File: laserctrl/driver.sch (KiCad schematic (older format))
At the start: 21 parts, among them IC4 DRV8811, P1 CONN_4

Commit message: Deleted the A-axis, it's getting too cramped with limited 328 I/O
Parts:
- C35: renamed from C64; value 100nF -> 1nF
- C36: renamed from C52; value 100nF -> 1nF
- R28: renamed from R44; value 1k -> 33k
- R29: renamed from R37; value 1k -> 33k
- R30: renamed from R38; value R -> 0R22
- R31: renamed from R39; value R -> 0R22
- gave numbers to parts that had none: 4
- renumbered C61 to C33, C51 to C34, C53 to C37, C54 to C38, C55 to C39, IC4 to IC7, JP1 to JP7, JP2 to JP8, P1 to P10, RV1 to RV7, RV2 to RV8
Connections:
- wire segments 70 -> 71
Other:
- moved on the sheet: D2, P3, R8, R9

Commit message: Actually did some work
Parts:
- removed RV7, RV8: 10k, symbol POT
- added C?: 100nF, symbol C
- added D?: LED, symbol LED
- added P?: CONN_2, symbol CONN_2
- added R? (x3): 10k, symbol R
- added R?: 330, symbol R
- added R?: 1k, symbol R
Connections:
- net labels added: +3.3V, Current, Max-Limit, Min-Limit
- net labels removed: +5V, Limit
- wire segments 71 -> 85
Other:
- note removed: "Current"
- note removed: "Decay\nmode"
- moved on the sheet: C12, C18, D2, P3, P4, R8, R9

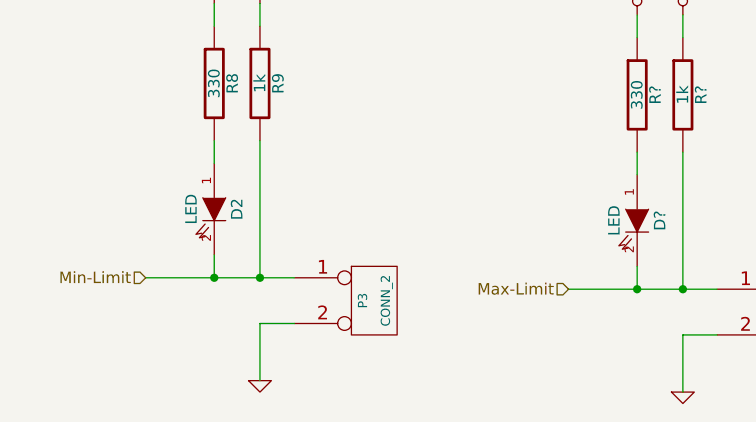
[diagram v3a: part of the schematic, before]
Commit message: Added laser interface schematic
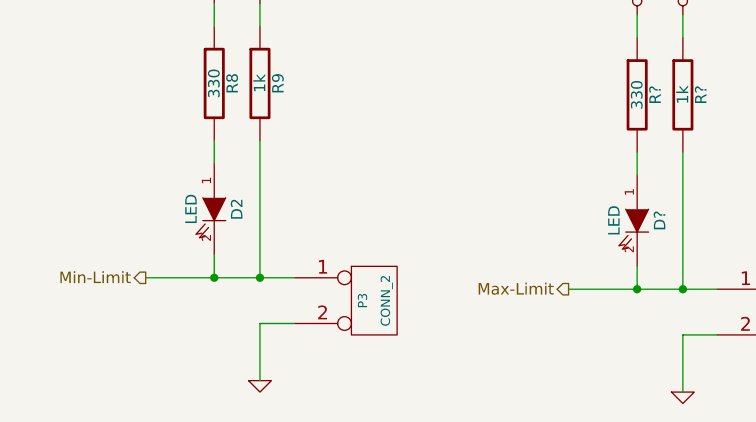
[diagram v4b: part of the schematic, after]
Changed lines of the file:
@@
-EESchema Schematic File Version 2  date 2011-10-30T14:11:45 CET
+EESchema Schematic File Version 2  date 2011-10-31T20:32:47 CET
 LIBS:power
 LIBS:device
@@
 EELAYER END
 $Descr A4 11700 8267
-Sheet 5 7
+Sheet 7 8
 Title ""
-Date "30 oct 2011"
+Date "31 oct 2011"
 Rev ""
 Comp ""
@@
 	0    1    1    0
 $EndComp
-Text HLabel 3400 7150 0    50   Input ~ 0
+Text HLabel 3400 7150 0    50   Output ~ 0
 Max-Limit
 $Comp
@@
 	-1   0    0    1
 $EndComp
-Text HLabel 1550 7100 0    50   Input ~ 0
+Text HLabel 1550 7100 0    50   Output ~ 0
 Min-Limit
 $Comp

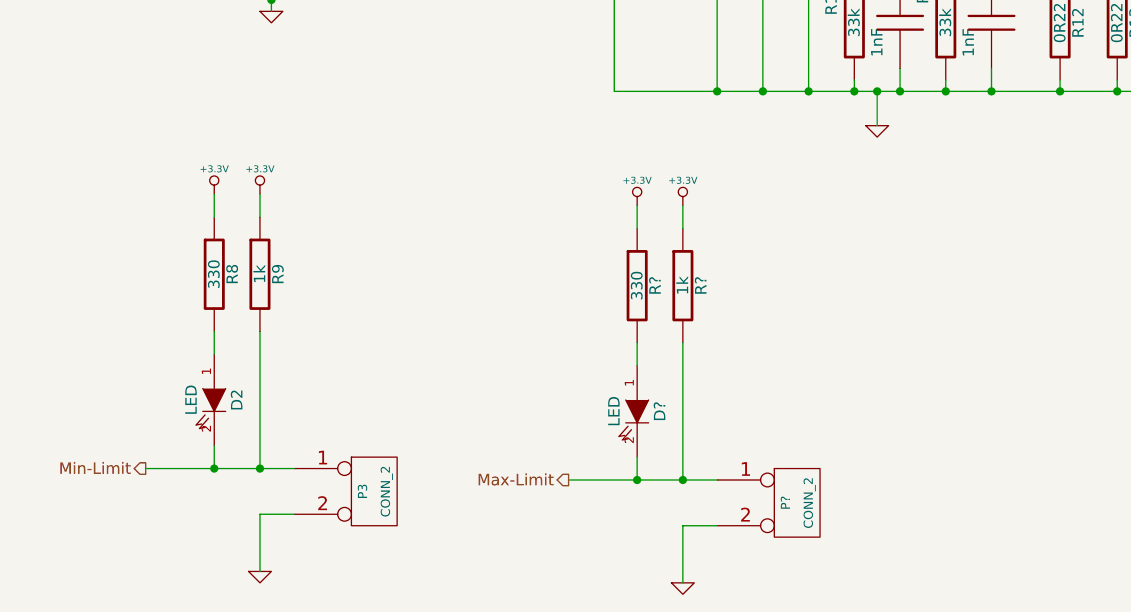
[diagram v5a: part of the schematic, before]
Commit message: Added transistors to drive the optocouplers
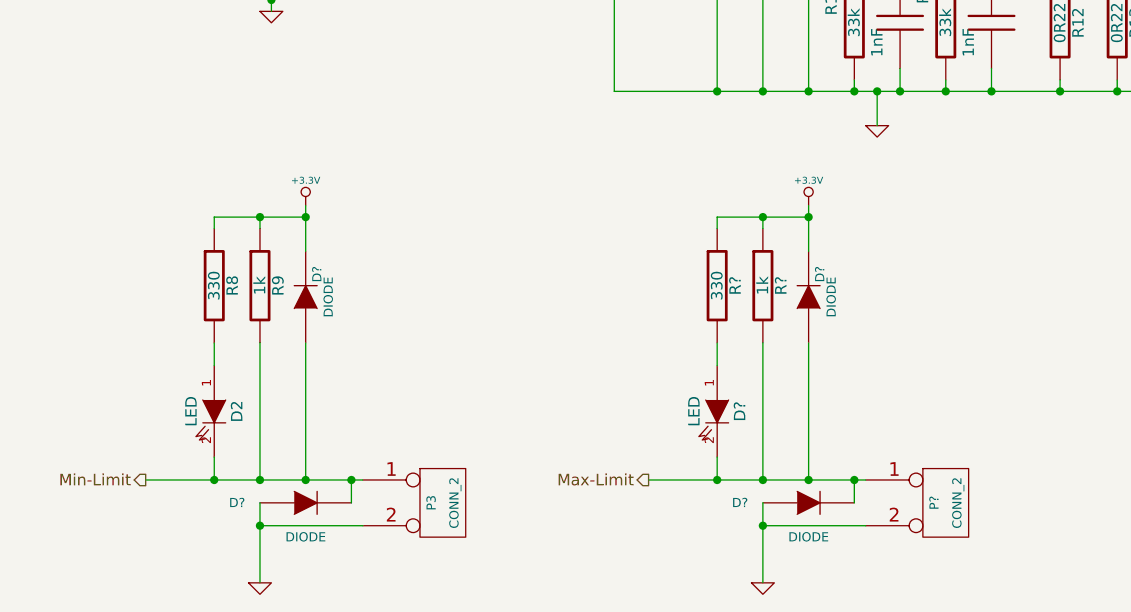
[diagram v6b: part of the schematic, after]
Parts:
- removed D?: LED, symbol LED
- removed P?: CONN_2, symbol CONN_2
- removed R?: 330, symbol R
- removed R?: 1k, symbol R
- added D? (x4): DIODE, symbol DIODE
- added D?: LED, symbol LED
- added P?: CONN_2, symbol CONN_2
- added R?: 330, symbol R
- added R?: 1k, symbol R
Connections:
- net +3.3V: now also D?.2 (K), D?.2 (K), R?.1, R?.1
- net GND: now also D?.1 (A), D?.1 (A), P?.2 (PM)
- net Max-Limit: now also D?.1 (A), D?.2 (K), D?.2 (K), P?.1 (P1), R?.2
- net Min-Limit: now also D?.1 (A), D?.2 (K)
- new net: D?.1 (A), R?.2
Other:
- moved on the sheet: D2, P3, R8, R9
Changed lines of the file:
@@
-EESchema Schematic File Version 2  date 2011-11-03T00:14:20 CET
+EESchema Schematic File Version 2  date 2011-11-04T21:23:22 CET
 LIBS:power
 LIBS:device
@@
 Sheet 7 8
 Title ""
-Date "2 nov 2011"
+Date "4 nov 2011"
 Rev ""
 Comp ""
@@
 Comment4 ""
 $EndDescr
+$Comp
+L GND #PWR?
+U 1 1 4EB44970
+P 4250 7600
+F 0 "#PWR?" H 4250 7600 30  0001 C CNN
+F 1 "GND" H 4250 7530 30  0001 C CNN
+	1    4250 7600
+	1    0    0    -1
+$EndComp
+$Comp
+L CONN_2 P?
+U 1 1 4EB4496F
+P 5050 7250
+F 0 "P?" V 5000 7250 40  0000 C CNN
+F 1 "CONN_2" V 5100 7250 40  0000 C CNN
+	1    5050 7250
+	1    0    0    -1
+$EndComp
+$Comp
+L R R?
+U 1 1 4EB4496E
+P 4250 6300
+F 0 "R?" V 4330 6300 50  0000 C CNN
+F 1 "1k" V 4250 6300 50  0000 C CNN
+	1    4250 6300
+	1    0    0    -1
+$EndComp
+$Comp
+L R R?
+U 1 1 4EB4496D
+P 4050 6300
+F 0 "R?" V 4130 6300 50  0000 C CNN
+F 1 "330" V 4050 6300 50  0000 C CNN
+	1    4050 6300
+	1    0    0    -1
+$EndComp
+$Comp
+L LED D?
+U 1 1 4EB4496C
+P 4050 6850
+F 0 "D?" H 4050 6950 50  0000 C CNN
+F 1 "LED" H 4050 6750 50  0000 C CNN
+	1    4050 6850
+	0    1    1    0
+$EndComp
+$Comp
+L +3.3V #PWR?
+U 1 1 4EB4496B
+P 4450 5950
+F 0 "#PWR?" H 4450 5910 30  0001 C CNN
+F 1 "+3.3V" H 4450 6060 30  0000 C CNN
+	1    4450 5950
+	1    0    0    -1
+$EndComp
+$Comp
+L DIODE D?
+U 1 1 4EB4496A
+P 4450 6350
+F 0 "D?" H 4550 6300 40  0000 C CNN
+F 1 "DIODE" H 4450 6250 40  0000 C CNN
+	1    4450 6350
+	0    -1   -1   0
+$EndComp
+$Comp
+L DIODE D?
+U 1 1 4EB44969
+P 4450 7250
+F 0 "D?" H 4150 7250 40  0000 C CNN
+F 1 "DIODE" H 4450 7100 40  0000 C CNN
+	1    4450 7250
+	1    0    0    -1
+$EndComp
+Connection ~ 4250 7350
+Wire Wire Line
+	4250 7250 4250 7600
+Connection ~ 4250 6000
+Wire Wire Line
+	4250 6050 4250 6000
+Wire Wire Line
+	4050 6000 4450 6000
+Connection ~ 4450 7150
+Wire Wire Line
+	4450 6550 4450 7150
+Wire Wire Line
+	4700 7150 3750 7150
+Wire Wire Line
+	4050 6550 4050 6650
+Connection ~ 4050 7150
+Wire Wire Line
+	4050 7150 4050 7050
+Wire Wire Line
+	4250 6550 4250 7150
+Connection ~ 4250 7150
+Wire Wire Line
+	4250 7350 4700 7350
+Wire Wire Line
+	4050 6050 4050 6000
+Wire Wire Line
+	4450 5950 4450 6150
+Connection ~ 4450 6000
+Wire Wire Line
+	4650 7250 4650 7150
+Connection ~ 4650 7150
+Connection ~ 2450 7150
+Wire Wire Line
+	2450 7250 2450 7150
+Connection ~ 2250 6000
+Wire Wire Line
+	2250 5950 2250 6150
+Wire Wire Line
+	1850 6050 1850 6000
+Wire Wire Line
+	2050 7350 2500 7350
 Wire Wire Line
 	5350 1700 5350 1850
-Wire Wire Line
-	3900 5950 3900 6050
-Wire Wire Line
-	3700 6550 3700 6650
-Connection ~ 3700 7150
-Wire Wire Line
-	4050 7150 3400 7150
-Wire Wire Line
-	3700 7150 3700 7050
-Wire Wire Line
-	3900 6550 3900 7150
-Connection ~ 3900 7150
-Wire Wire Line
-	3700 6050 3700 5950
-Wire Wire Line
-	3900 7600 3900 7350
-Wire Wire Line
-	3900 7350 4050 7350
 Wire Wire Line
 	2700 4000 2750 4000
@@
 Wire Wire Line
 	6050 5450 3600 5450
-Wire Wire Line
-	2200 7300 2050 7300
-Wire Wire Line
-	2050 7300 2050 7550
-Wire Wire Line
-	1850 6000 1850 5900
-Connection ~ 2050 7100
-Wire Wire Line
-	2050 6500 2050 7100
-Wire Wire Line
-	1850 7100 1850 7000
+Connection ~ 2050 7150
+Wire Wire Line
+	2050 6550 2050 7150
+Wire Wire Line
+	1850 7150 1850 7050
 Wire Wire Line
 	3650 3400 1650 3400
@@
 Wire Wire Line
 	3650 3600 1650 3600
-Wire Wire Line
-	2200 7100 1550 7100
-Connection ~ 1850 7100
-Wire Wire Line
-	1850 6500 1850 6600
-Wire Wire Line
-	2050 5900 2050 6000
+Connection ~ 1850 7150
+Wire Wire Line
+	1850 6550 1850 6650
 Wire Wire Line
 	4050 4750 4050 5450
@@
 Wire Wire Line
 	5150 1150 5150 1850
-$Comp
-L GND #PWR?
-U 1 1 4EAD2CF1
-P 3900 7600
-F 0 "#PWR?" H 3900 7600 30  0001 C CNN
-F 1 "GND" H 3900 7530 30  0001 C CNN
-	1    3900 7600
-	1    0    0    -1
-$EndComp
-$Comp
-L CONN_2 P?
-U 1 1 4EAD2CF0
-P 4400 7250
-F 0 "P?" V 4350 7250 40  0000 C CNN
-F 1 "CONN_2" V 4450 7250 40  0000 C CNN
-	1    4400 7250
-	1    0    0    -1
-$EndComp
-$Comp
-L R R?
-U 1 1 4EAD2CEF
-P 3900 6300
-F 0 "R?" V 3980 6300 50  0000 C CNN
-F 1 "1k" V 3900 6300 50  0000 C CNN
-	1    3900 6300
-	1    0    0    -1
-$EndComp
-$Comp
-L R R?
-U 1 1 4EAD2CEE
-P 3700 6300
-F 0 "R?" V 3780 6300 50  0000 C CNN
-F 1 "330" V 3700 6300 50  0000 C CNN
-	1    3700 6300
-	1    0    0    -1
-$EndComp
-$Comp
-L LED D?
-U 1 1 4EAD2CED
-P 3700 6850
-F 0 "D?" H 3700 6950 50  0000 C CNN
-F 1 "LED" H 3700 6750 50  0000 C CNN
-	1    3700 6850
-	0    1    1    0
-$EndComp
-Text HLabel 3400 7150 0    50   Output ~ 0
+Wire Wire Line
+	2500 7150 1550 7150
+Wire Wire Line
+	2250 6550 2250 7150
+Connection ~ 2250 7150
+Wire Wire Line
+	1850 6000 2250 6000
+Wire Wire Line
+	2050 6050 2050 6000
+Connection ~ 2050 6000
+Wire Wire Line
+	2050 7250 2050 7600
+Connection ~ 2050 7350
+$Comp
+L DIODE D?
+U 1 1 4EB4493E
+P 2250 7250
+F 0 "D?" H 1950 7250 40  0000 C CNN
+F 1 "DIODE" H 2250 7100 40  0000 C CNN
+	1    2250 7250
+	1    0    0    -1
+$EndComp
+$Comp
+L DIODE D?
+U 1 1 4EB448E5
+P 2250 6350
+F 0 "D?" H 2350 6300 40  0000 C CNN
+F 1 "DIODE" H 2250 6250 40  0000 C CNN
+	1    2250 6350
+	0    -1   -1   0
+$EndComp
+Text HLabel 3750 7150 0    50   Output ~ 0
 Max-Limit
-$Comp
-L +3.3V #PWR?
-U 1 1 4EAD2CEC
-P 3900 5950
-F 0 "#PWR?" H 3900 5910 30  0001 C CNN
-F 1 "+3.3V" H 3900 6060 30  0000 C CNN
-	1    3900 5950
-	1    0    0    -1
-$EndComp
-$Comp
-L +3.3V #PWR?
-U 1 1 4EAD2CEB
-P 3700 5950
-F 0 "#PWR?" H 3700 5910 30  0001 C CNN
-F 1 "+3.3V" H 3700 6060 30  0000 C CNN
-	1    3700 5950
-	1    0    0    -1
-$EndComp
 $Comp
 L +3.3V #PWR?
@@
 $Comp
 L +3.3V #PWR?
-U 1 1 4EAD2C67
-P 1850 5900
-F 0 "#PWR?" H 1850 5860 30  0001 C CNN
-F 1 "+3.3V" H 1850 6010 30  0000 C CNN
-	1    1850 5900
-	1    0    0    -1
-$EndComp
-$Comp
-L +3.3V #PWR?
 U 1 1 4EAD2C61
-P 2050 5900
-F 0 "#PWR?" H 2050 5860 30  0001 C CNN
-F 1 "+3.3V" H 2050 6010 30  0000 C CNN
-	1    2050 5900
+P 2250 5950
+F 0 "#PWR?" H 2250 5910 30  0001 C CNN
+F 1 "+3.3V" H 2250 6060 30  0000 C CNN
+	1    2250 5950
 	1    0    0    -1
 $EndComp
@@
 	-1   0    0    1
 $EndComp
-Text HLabel 1550 7100 0    50   Output ~ 0
+Text HLabel 1550 7150 0    50   Output ~ 0
 Min-Limit
 $Comp
 L LED D5
 U 1 1 4EA29348
-P 1850 6800
+P 1850 6850
 AR Path="/4EA1F594/4EA29348" Ref="D5"  Part="1"
 AR Path="/4EA1F56E/4EA29348" Ref="D4"  Part="1"
 AR Path="/4EA1D353/4EA29348" Ref="D3"  Part="1"
 AR Path="/4EA1D331/4EA29348" Ref="D2"  Part="1"
-F 0 "D2" H 1850 6900 50  0000 C CNN
-F 1 "LED" H 1850 6700 50  0000 C CNN
-	1    1850 6800
+F 0 "D2" H 1850 6950 50  0000 C CNN
+F 1 "LED" H 1850 6750 50  0000 C CNN
+	1    1850 6850
 	0    1    1    0
 $EndComp
@@
 L R R26
 U 1 1 4EA29337
-P 1850 6250
+P 1850 6300
 AR Path="/4EA1F594/4EA29337" Ref="R26"  Part="1"
 AR Path="/4EA1F56E/4EA29337" Ref="R20"  Part="1"
 AR Path="/4EA1D353/4EA29337" Ref="R14"  Part="1"
 AR Path="/4EA1D331/4EA29337" Ref="R8"  Part="1"
-F 0 "R8" V 1930 6250 50  0000 C CNN
-F 1 "330" V 1850 6250 50  0000 C CNN
-	1    1850 6250
+F 0 "R8" V 1930 6300 50  0000 C CNN
+F 1 "330" V 1850 6300 50  0000 C CNN
+	1    1850 6300
 	1    0    0    -1
 $EndComp
@@
 L R R27
 U 1 1 4EA2931D
-P 2050 6250
+P 2050 6300
 AR Path="/4EA1F594/4EA2931D" Ref="R27"  Part="1"
 AR Path="/4EA1F56E/4EA2931D" Ref="R21"  Part="1"
 AR Path="/4EA1D353/4EA2931D" Ref="R15"  Part="1"
 AR Path="/4EA1D331/4EA2931D" Ref="R9"  Part="1"
-F 0 "R9" V 2130 6250 50  0000 C CNN
-F 1 "1k" V 2050 6250 50  0000 C CNN
-	1    2050 6250
+F 0 "R9" V 2130 6300 50  0000 C CNN
+F 1 "1k" V 2050 6300 50  0000 C CNN
+	1    2050 6300
 	1    0    0    -1
 $EndComp
@@
 L CONN_2 P9
 U 1 1 4EA29315
-P 2550 7200
+P 2850 7250
 AR Path="/4EA1F594/4EA29315" Ref="P9"  Part="1"
 AR Path="/4EA1F56E/4EA29315" Ref="P7"  Part="1"
 AR Path="/4EA1D353/4EA29315" Ref="P5"  Part="1"
 AR Path="/4EA1D331/4EA29315" Ref="P3"  Part="1"
-F 0 "P3" V 2500 7200 40  0000 C CNN
-F 1 "CONN_2" V 2600 7200 40  0000 C CNN
-	1    2550 7200
+F 0 "P3" V 2800 7250 40  0000 C CNN
+F 1 "CONN_2" V 2900 7250 40  0000 C CNN
+	1    2850 7250
 	1    0    0    -1
 $EndComp
@@
 L GND #PWR69
 U 1 1 4EA29310
-P 2050 7550
+P 2050 7600
 AR Path="/4EA1F594/4EA29310" Ref="#PWR69"  Part="1"
 AR Path="/4EA1F56E/4EA29310" Ref="#PWR58"  Part="1"
 AR Path="/4EA1D353/4EA29310" Ref="#PWR47"  Part="1"
 AR Path="/4EA1D331/4EA29310" Ref="#PWR36"  Part="1"
-F 0 "#PWR36" H 2050 7550 30  0001 C CNN
-F 1 "GND" H 2050 7480 30  0001 C CNN
-	1    2050 7550
-	1    0    0    -1
-$EndComp
+F 0 "#PWR36" H 2050 7600 30  0001 C CNN
+F 1 "GND" H 2050 7530 30  0001 C CNN
+	1    2050 7600
+	1    0    0    -1
+$EndComp

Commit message: Added NTC sensors
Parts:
- removed D5: LED, symbol LED
- removed D? (x2): DIODE, symbol DIODE
- removed P9: CONN_2, symbol CONN_2
- removed R26: 330, symbol R
- removed R27: 1k, symbol R
- added C? (x2): 10nF, symbol C
- added C? (x2): 10uF, symbol C
- added C?: 100nF, symbol C
- added C?: 220uF, symbol CAPAPOL
- added D?: LED, symbol LED
- added D? (x2): DIODE, symbol DIODE
- added P?: CONN_2, symbol CONN_2
- added R?: 1k, symbol R
- added R?: 330, symbol R
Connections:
- net +24V: now also C?.1, C?.1, C?.1
- net +3.3V: now also C?.1, D?.2 (K), R?.1, R?.1
- net GND: now also C?.2, C?.2, C?.2, C?.2, C?.2, C?.2, D?.1 (A), P?.2 (PM)
- net Max-Limit: now also C?.1
- net Min-Limit: now also C?.1, D?.1 (A), D?.2 (K), D?.2 (K), P?.1 (P1), R?.2
- new net: D?.1 (A), R?.2
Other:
- moved on the sheet: D?
